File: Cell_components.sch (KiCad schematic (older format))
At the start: 12 parts, among them Q6 BUK9M20-40HX

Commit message: Add files via upload
Additional back-up before starting Rev.1
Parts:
- removed Q6: BUK9M20-40HX, Package_TO_SOT_SMD:LFPAK33, symbol Transistor_FET:BUK9M9R1-40EX
- added Q6: Q_NMOS_GSD, Package_TO_SOT_SMD:SOT-23, symbol Device:Q_NMOS_GSD
- C11, C12: DPN 710-885012207128 -> (none); LCSC (none) -> C49678
- D11, D12: DPN 771-PDZ5.6BGWJ -> (none); LCSC (none) -> C173406
- D16: footprint LED_SMD:LED_0603_1608Metric_Pad1.05x0.95mm_HandSolder -> LED_SMD:LED_0805_2012Metric_Pad1.15x1.40mm_HandSolder; LCSC (none) -> C2296
- R1, R3: DPN 603-RT0603FRE071KL -> (none); LCSC (none) -> C21190
- R19, R20: value 47 -> 51; DPN 652-CMP2512AFX-47R0L -> (none); LCSC (none) -> C41977
- R2: DPN 71-CRCW08051M00FKEAC -> (none); LCSC (none) -> C17514
- R31: value ?? -> 1k; DPN 603-RT0603FRE071KL -> (none); LCSC (none) -> C21190
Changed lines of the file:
@@
 $Descr User 7874 5906
 encoding utf-8
-Sheet 2 7
+Sheet 5 7
 Title ""
 Date ""
@@
 Comment4 ""
 $EndDescr
-$Comp
-L Transistor_FET:BUK9M9R1-40EX Q6
-U 1 1 5FB0C1EB
-P 3750 2200
-AR Path="/5FAA7870/5FB0C1EB" Ref="Q6"  Part="1"
-AR Path="/5FAF2B15/5FB0C1EB" Ref="Q2"  Part="1"
-AR Path="/5FB201DB/5FB0C1EB" Ref="Q1"  Part="1"
-AR Path="/5FB24C66/5FB0C1EB" Ref="Q3"  Part="1"
-AR Path="/5FA9BBC5/5FB0C1EB" Ref="Q4"  Part="1"
-AR Path="/5FA9D4E1/5FB0C1EB" Ref="Q5"  Part="1"
-F 0 "Q6" H 3600 2450 50  0000 L CNN
-F 1 "BUK9M20-40HX" H 3100 2350 50  0000 L CNN
-F 2 "Package_TO_SOT_SMD:LFPAK33" H 3950 2125 50  0001 L CIN
-F 3 "file:///C:/Users/HenkHenk/Downloads/BUK9M20-40H-1599146%20(1).pdf" V 3750 2200 50  0001 L CNN
-F 4 "771-BUK9M20-40HX" H 3750 2200 50  0001 C CNN "DPN"
-	1    3750 2200
-	-1   0    0    -1
-$EndComp
 Text HLabel 1700 1500 0    50   UnSpc ~ 0
 S+
@@
 AR Path="/5FA9BBC5/5FB16918" Ref="C8"  Part="1"
 AR Path="/5FA9D4E1/5FB16918" Ref="C10"  Part="1"
-F 0 "C12" H 1965 2096 50  0000 L CNN
+F 0 "C8" H 1965 2096 50  0000 L CNN
 F 1 "0.1u " H 1965 2005 50  0000 L CNN
 F 2 "Capacitor_SMD:C_0805_2012Metric_Pad1.15x1.40mm_HandSolder" H 1888 1900 50  0001 C CNN
 F 3 "file:///C:/Users/HenkHenk/Downloads/885012207128-1727772.pdf" H 1850 2050 50  0001 C CNN
-F 4 "710-885012207128" H 1850 2050 50  0001 C CNN "DPN"
+F 4 "C49678" H 1850 2050 50  0001 C CNN "LCSC"
 	1    1850 2050
 	1    0    0    -1
@@
 AR Path="/5FA9BBC5/5FB1FCF3" Ref="C7"  Part="1"
 AR Path="/5FA9D4E1/5FB1FCF3" Ref="C9"  Part="1"
-F 0 "C11" H 5365 1746 50  0000 L CNN
+F 0 "C7" H 5365 1746 50  0000 L CNN
 F 1 "0.1u " H 5365 1655 50  0000 L CNN
 F 2 "Capacitor_SMD:C_0805_2012Metric_Pad1.15x1.40mm_HandSolder" H 5288 1550 50  0001 C CNN
 F 3 "file:///C:/Users/HenkHenk/Downloads/885012207128-1727772.pdf" H 5250 1700 50  0001 C CNN
-F 4 "710-885012207128" H 5250 1700 50  0001 C CNN "DPN"
+F 4 "C49678" H 5250 1700 50  0001 C CNN "LCSC"
 	1    5250 1700
 	1    0    0    -1
@@
 AR Path="/5FA9D4E1/5FB211C7" Ref="R15"  Part="1"
 AR Path="/5FAA7870/5FB211C7" Ref="R18"  Part="1"
-F 0 "R18" V 5150 1450 50  0000 L CNN
+F 0 "R12" V 5150 1450 50  0000 L CNN
 F 1 "1K" V 5050 1450 50  0000 L CNN
 F 2 "Resistor_SMD:R_0603_1608Metric_Pad1.05x0.95mm_HandSolder" V 4880 1500 50  0001 C CNN
 F 3 "~" H 4950 1500 50  0001 C CNN
-F 4 "603-RT0603FRE071KL" V 4950 1500 50  0001 C CNN "DPN"
+F 4 "C21190" V 4950 1500 50  0001 C CNN "LCSC"
 	1    4950 1500
 	0    -1   -1   0
@@
 AR Path="/5FA9D4E1/5FB24803" Ref="R13"  Part="1"
 AR Path="/5FAA7870/5FB24803" Ref="R16"  Part="1"
-F 0 "R16" V 5150 2150 50  0000 L CNN
+F 0 "R10" V 5150 2150 50  0000 L CNN
 F 1 "1K" V 5050 2150 50  0000 L CNN
 F 2 "Resistor_SMD:R_0603_1608Metric_Pad1.05x0.95mm_HandSolder" V 4880 2200 50  0001 C CNN
 F 3 "~" H 4950 2200 50  0001 C CNN
-F 4 "603-RT0603FRE071KL" V 4950 2200 50  0001 C CNN "DPN"
+F 4 "C21190" V 4950 2200 50  0001 C CNN "LCSC"
 	1    4950 2200
 	0    -1   -1   0
@@
 AR Path="/5FA9D4E1/5FB273BA" Ref="R14"  Part="1"
 AR Path="/5FAA7870/5FB273BA" Ref="R17"  Part="1"
-F 0 "R17" H 4300 2350 50  0000 L CNN
+F 0 "R11" H 4300 2350 50  0000 L CNN
 F 1 "1M" H 4300 2450 50  0000 L CNN
 F 2 "Resistor_SMD:R_0805_2012Metric_Pad1.15x1.40mm_HandSolder" V 4430 2400 50  0001 C CNN
 F 3 "~" H 4500 2400 50  0001 C CNN
-F 4 "71-CRCW08051M00FKEAC" H 4500 2400 50  0001 C CNN "DPN"
+F 4 "C17514" H 4500 2400 50  0001 C CNN "LCSC"
 	1    4500 2400
 	-1   0    0    1
@@
 AR Path="/5FA9BBC5/5FB3410E" Ref="D7"  Part="1"
 AR Path="/5FA9D4E1/5FB3410E" Ref="D9"  Part="1"
-F 0 "D11" V 2354 2130 50  0000 L CNN
+F 0 "D7" V 2354 2130 50  0000 L CNN
 F 1 "5V6" V 2445 2130 50  0000 L CNN
 F 2 "Diode_SMD:D_SOD-123" H 2400 2050 50  0001 C CNN
 F 3 "file:///C:/Users/HenkHenk/Downloads/PDZ-GW_SER-1599748.pdf" H 2400 2050 50  0001 C CNN
-F 4 "771-PDZ5.6BGWJ" V 2400 2050 50  0001 C CNN "DPN"
+F 4 "C173406" V 2400 2050 50  0001 C CNN "LCSC"
 	1    2400 2050
 	0    1    1    0
@@
 AR Path="/5FA9BBC5/5FB35DA2" Ref="D8"  Part="1"
 AR Path="/5FA9D4E1/5FB35DA2" Ref="D10"  Part="1"
-F 0 "D12" V 4104 2480 50  0000 L CNN
+F 0 "D8" V 4104 2480 50  0000 L CNN
 F 1 "5V6" V 4195 2480 50  0000 L CNN
 F 2 "Diode_SMD:D_SOD-123" H 4150 2400 50  0001 C CNN
 F 3 "file:///C:/Users/HenkHenk/Downloads/PDZ-GW_SER-1599748.pdf" H 4150 2400 50  0001 C CNN
-F 4 "771-PDZ5.6BGWJ" V 4150 2400 50  0001 C CNN "DPN"
+F 4 "C173406" V 4150 2400 50  0001 C CNN "LCSC"
 	1    4150 2400
 	0    1    1    0
@@
 AR Path="/5FA9D4E1/5FAFC2A5" Ref="R28"  Part="1"
 AR Path="/5FAA7870/5FAFC2A5" Ref="R30"  Part="1"
-F 0 "R30" H 3500 1700 50  0000 L CNN
-F 1 "47" H 3500 1800 50  0000 L CNN
+F 0 "R26" H 3500 1700 50  0000 L CNN
+F 1 "51" H 3500 1800 50  0000 L CNN
 F 2 "Resistor_SMD:R_2512_6332Metric_Pad1.52x3.35mm_HandSolder" V 3580 1750 50  0001 C CNN
 F 3 "file:///C:/Users/HenkHenk/Downloads/cmp-a.pdf" H 3650 1750 50  0001 C CNN
-F 4 "652-CMP2512AFX-47R0L" V 3650 1750 50  0001 C CNN "DPN"
+F 4 "C41977" V 3650 1750 50  0001 C CNN "LCSC"
 	1    3650 1750
 	-1   0    0    1
@@
 AR Path="/5FA9D4E1/5FAFE41B" Ref="R27"  Part="1"
 AR Path="/5FAA7870/5FAFE41B" Ref="R29"  Part="1"
-F 0 "R29" H 3250 1700 50  0000 L CNN
-F 1 "47" H 3250 1800 50  0000 L CNN
+F 0 "R25" H 3250 1700 50  0000 L CNN
+F 1 "51" H 3250 1800 50  0000 L CNN
 F 2 "Resistor_SMD:R_2512_6332Metric_Pad1.52x3.35mm_HandSolder" V 3330 1750 50  0001 C CNN
 F 3 "file:///C:/Users/HenkHenk/Downloads/cmp-a.pdf" H 3400 1750 50  0001 C CNN
-F 4 "652-CMP2512AFX-47R0L" V 3400 1750 50  0001 C CNN "DPN"
+F 4 "C41977" V 3400 1750 50  0001 C CNN "LCSC"
 	1    3400 1750
 	-1   0    0    1
@@
 AR Path="/5FA9D4E1/5FB07EF1" Ref="R35"  Part="1"
 AR Path="/5FAA7870/5FB07EF1" Ref="R36"  Part="1"
-F 0 "R36" V 3050 1700 50  0000 L CNN
-F 1 "??" V 2950 1700 50  0000 L CNN
+F 0 "R34" V 3050 1700 50  0000 L CNN
+F 1 "1k" V 2950 1700 50  0000 L CNN
 F 2 "Resistor_SMD:R_0603_1608Metric_Pad1.05x0.95mm_HandSolder" V 2780 1750 50  0001 C CNN
 F 3 "~" H 2850 1750 50  0001 C CNN
-F 4 "603-RT0603FRE071KL" V 2850 1750 50  0001 C CNN "DPN"
+F 4 "C21190" V 2850 1750 50  0001 C CNN "LCSC"
 	1    2850 1750
 	-1   0    0    1
@@
 AR Path="/5FA9D4E1/5FB0934F" Ref="D17"  Part="1"
 AR Path="/5FAA7870/5FB0934F" Ref="D18"  Part="1"
-F 0 "D18" H 3093 1695 50  0000 C CNN
+F 0 "D16" H 3093 1695 50  0000 C CNN
 F 1 "LED" H 3093 1786 50  0000 C CNN
-F 2 "LED_SMD:LED_0603_1608Metric_Pad1.05x0.95mm_HandSolder" H 3100 1950 50  0001 C CNN
+F 2 "LED_SMD:LED_0805_2012Metric_Pad1.15x1.40mm_HandSolder" H 3100 1950 50  0001 C CNN
 F 3 "~" H 3100 1950 50  0001 C CNN
+F 4 "C2296" H 3100 1950 50  0001 C CNN "LCSC"
 	1    3100 1950
 	-1   0    0    1
@@
 	3250 1950 3400 1950
 Connection ~ 3400 1950
+$Comp
+L Device:Q_NMOS_GSD Q6
+U 1 1 601F5F7C
+P 3750 2200
+AR Path="/5FAA7870/601F5F7C" Ref="Q6"  Part="1"
+AR Path="/5FAF2B15/601F5F7C" Ref="Q1"  Part="1"
+AR Path="/5FB201DB/601F5F7C" Ref="Q2"  Part="1"
+AR Path="/5FB24C66/601F5F7C" Ref="Q3"  Part="1"
+AR Path="/5FA9BBC5/601F5F7C" Ref="Q4"  Part="1"
+AR Path="/5FA9D4E1/601F5F7C" Ref="Q5"  Part="1"
+F 0 "Q4" H 3955 2246 50  0000 L CNN
+F 1 "Q_NMOS_GSD" H 3955 2155 50  0000 L CNN
+F 2 "Package_TO_SOT_SMD:SOT-23" H 3950 2300 50  0001 C CNN
+F 3 "~" H 3750 2200 50  0001 C CNN
+F 4 "C20917" H 3750 2200 50  0001 C CNN "LCSC"
+	1    3750 2200
+	-1   0    0    -1
+$EndComp
 $EndSCHEMATC

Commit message: Add files via upload
Changed board dimensions. Replaced Molex connectors from MiniFit to the smaller MicroFit-type.
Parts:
- renumbered C12 to C23, C11 to C24, D16 to D11, D11 to D16, D12 to D18, R31 to R4, R19 to R5, R20 to R6, R2 to R7, R3 to R8, R1 to R9

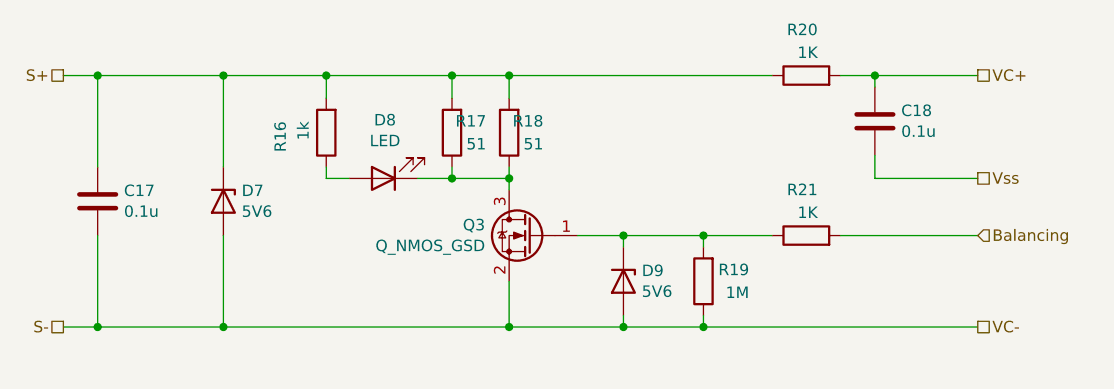
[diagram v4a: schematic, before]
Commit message: Add files via upload
Placed most components. Started routing and placing vias.
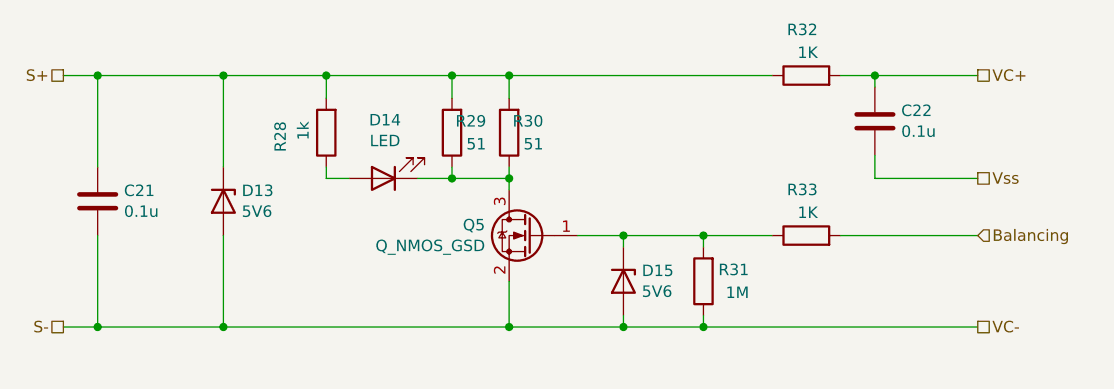
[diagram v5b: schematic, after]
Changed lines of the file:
@@
 $Descr User 7874 5906
 encoding utf-8
-Sheet 4 7
+Sheet 6 7
 Title ""
 Date ""
@@
 AR Path="/5FA9BBC5/5FB16918" Ref="C19"  Part="1"
 AR Path="/5FA9D4E1/5FB16918" Ref="C21"  Part="1"
-F 0 "C17" H 1965 2096 50  0000 L CNN
+F 0 "C21" H 1965 2096 50  0000 L CNN
 F 1 "0.1u " H 1965 2005 50  0000 L CNN
 F 2 "Capacitor_SMD:C_0805_2012Metric_Pad1.15x1.40mm_HandSolder" H 1888 1900 50  0001 C CNN
@@
 AR Path="/5FA9BBC5/5FB1FCF3" Ref="C20"  Part="1"
 AR Path="/5FA9D4E1/5FB1FCF3" Ref="C22"  Part="1"
-F 0 "C18" H 5365 1746 50  0000 L CNN
+F 0 "C22" H 5365 1746 50  0000 L CNN
 F 1 "0.1u " H 5365 1655 50  0000 L CNN
 F 2 "Capacitor_SMD:C_0805_2012Metric_Pad1.15x1.40mm_HandSolder" H 5288 1550 50  0001 C CNN
@@
 AR Path="/5FA9D4E1/5FB211C7" Ref="R32"  Part="1"
 AR Path="/5FAA7870/5FB211C7" Ref="R38"  Part="1"
-F 0 "R20" V 5150 1450 50  0000 L CNN
+F 0 "R32" V 5150 1450 50  0000 L CNN
 F 1 "1K" V 5050 1450 50  0000 L CNN
 F 2 "Resistor_SMD:R_0603_1608Metric_Pad1.05x0.95mm_HandSolder" V 4880 1500 50  0001 C CNN
@@
 AR Path="/5FA9D4E1/5FB24803" Ref="R33"  Part="1"
 AR Path="/5FAA7870/5FB24803" Ref="R39"  Part="1"
-F 0 "R21" V 5150 2150 50  0000 L CNN
+F 0 "R33" V 5150 2150 50  0000 L CNN
 F 1 "1K" V 5050 2150 50  0000 L CNN
 F 2 "Resistor_SMD:R_0603_1608Metric_Pad1.05x0.95mm_HandSolder" V 4880 2200 50  0001 C CNN
@@
 AR Path="/5FA9D4E1/5FB273BA" Ref="R31"  Part="1"
 AR Path="/5FAA7870/5FB273BA" Ref="R37"  Part="1"
-F 0 "R19" H 4300 2350 50  0000 L CNN
+F 0 "R31" H 4300 2350 50  0000 L CNN
 F 1 "1M" H 4300 2450 50  0000 L CNN
 F 2 "Resistor_SMD:R_0805_2012Metric_Pad1.15x1.40mm_HandSolder" V 4430 2400 50  0001 C CNN
@@
 AR Path="/5FA9BBC5/5FB35DA2" Ref="D12"  Part="1"
 AR Path="/5FA9D4E1/5FB35DA2" Ref="D15"  Part="1"
-F 0 "D9" V 4104 2480 50  0000 L CNN
+F 0 "D15" V 4104 2480 50  0000 L CNN
 F 1 "5V6" V 4195 2480 50  0000 L CNN
 F 2 "Diode_SMD:D_SOD-123" H 4150 2400 50  0001 C CNN
@@
 AR Path="/5FA9D4E1/5FAFC2A5" Ref="R30"  Part="1"
 AR Path="/5FAA7870/5FAFC2A5" Ref="R36"  Part="1"
-F 0 "R18" H 3500 1700 50  0000 L CNN
+F 0 "R30" H 3500 1700 50  0000 L CNN
 F 1 "51" H 3500 1800 50  0000 L CNN
 F 2 "Resistor_SMD:R_2512_6332Metric_Pad1.52x3.35mm_HandSolder" V 3580 1750 50  0001 C CNN
@@
 AR Path="/5FA9D4E1/5FAFE41B" Ref="R29"  Part="1"
 AR Path="/5FAA7870/5FAFE41B" Ref="R35"  Part="1"
-F 0 "R17" H 3250 1700 50  0000 L CNN
+F 0 "R29" H 3250 1700 50  0000 L CNN
 F 1 "51" H 3250 1800 50  0000 L CNN
 F 2 "Resistor_SMD:R_2512_6332Metric_Pad1.52x3.35mm_HandSolder" V 3330 1750 50  0001 C CNN
@@
 AR Path="/5FA9D4E1/5FB07EF1" Ref="R28"  Part="1"
 AR Path="/5FAA7870/5FB07EF1" Ref="R34"  Part="1"
-F 0 "R16" V 3050 1700 50  0000 L CNN
+F 0 "R28" V 3050 1700 50  0000 L CNN
 F 1 "1k" V 2950 1700 50  0000 L CNN
 F 2 "Resistor_SMD:R_0603_1608Metric_Pad1.05x0.95mm_HandSolder" V 2780 1750 50  0001 C CNN
@@
 AR Path="/5FA9D4E1/5FB0934F" Ref="D14"  Part="1"
 AR Path="/5FAA7870/5FB0934F" Ref="D17"  Part="1"
-F 0 "D8" H 3093 1695 50  0000 C CNN
+F 0 "D14" H 3093 1695 50  0000 C CNN
 F 1 "LED" H 3093 1786 50  0000 C CNN
 F 2 "LED_SMD:LED_0805_2012Metric_Pad1.15x1.40mm_HandSolder" H 3100 1950 50  0001 C CNN
@@
 AR Path="/5FA9BBC5/601F5F7C" Ref="Q4"  Part="1"
 AR Path="/5FA9D4E1/601F5F7C" Ref="Q5"  Part="1"
-F 0 "Q3" H 3955 2246 50  0000 L CNN
+F 0 "Q5" H 3955 2246 50  0000 L CNN
 F 1 "Q_NMOS_GSD" H 3955 2155 50  0000 L CNN
 F 2 "Package_TO_SOT_SMD:SOT-23" H 3950 2300 50  0001 C CNN
@@
 AR Path="/5FA9BBC5/5FB3410E" Ref="D10"  Part="1"
 AR Path="/5FA9D4E1/5FB3410E" Ref="D13"  Part="1"
-F 0 "D7" V 2354 2130 50  0000 L CNN
+F 0 "D13" V 2354 2130 50  0000 L CNN
 F 1 "5V6" V 2445 2130 50  0000 L CNN
 F 2 "Diode_SMD:D_SOD-123" H 2400 2050 50  0001 C CNN

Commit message: Add files via upload
Routed external thermistor and HOST-interface traces. Added silkscreen text. Placed additional AGND-via's.
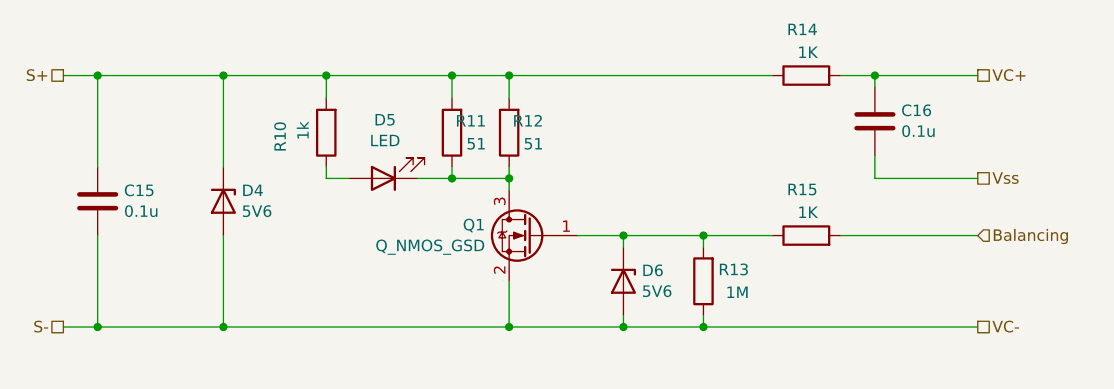
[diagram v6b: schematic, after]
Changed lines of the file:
@@
 $Descr User 7874 5906
 encoding utf-8
-Sheet 6 7
+Sheet 3 7
 Title ""
 Date ""
@@
 AR Path="/5FA9BBC5/5FB16918" Ref="C19"  Part="1"
 AR Path="/5FA9D4E1/5FB16918" Ref="C21"  Part="1"
-F 0 "C21" H 1965 2096 50  0000 L CNN
+F 0 "C15" H 1965 2096 50  0000 L CNN
 F 1 "0.1u " H 1965 2005 50  0000 L CNN
 F 2 "Capacitor_SMD:C_0805_2012Metric_Pad1.15x1.40mm_HandSolder" H 1888 1900 50  0001 C CNN
@@
 AR Path="/5FA9BBC5/5FB1FCF3" Ref="C20"  Part="1"
 AR Path="/5FA9D4E1/5FB1FCF3" Ref="C22"  Part="1"
-F 0 "C22" H 5365 1746 50  0000 L CNN
+F 0 "C16" H 5365 1746 50  0000 L CNN
 F 1 "0.1u " H 5365 1655 50  0000 L CNN
 F 2 "Capacitor_SMD:C_0805_2012Metric_Pad1.15x1.40mm_HandSolder" H 5288 1550 50  0001 C CNN
@@
 AR Path="/5FA9D4E1/5FB211C7" Ref="R32"  Part="1"
 AR Path="/5FAA7870/5FB211C7" Ref="R38"  Part="1"
-F 0 "R32" V 5150 1450 50  0000 L CNN
+F 0 "R14" V 5150 1450 50  0000 L CNN
 F 1 "1K" V 5050 1450 50  0000 L CNN
 F 2 "Resistor_SMD:R_0603_1608Metric_Pad1.05x0.95mm_HandSolder" V 4880 1500 50  0001 C CNN
@@
 AR Path="/5FA9D4E1/5FB24803" Ref="R33"  Part="1"
 AR Path="/5FAA7870/5FB24803" Ref="R39"  Part="1"
-F 0 "R33" V 5150 2150 50  0000 L CNN
+F 0 "R15" V 5150 2150 50  0000 L CNN
 F 1 "1K" V 5050 2150 50  0000 L CNN
 F 2 "Resistor_SMD:R_0603_1608Metric_Pad1.05x0.95mm_HandSolder" V 4880 2200 50  0001 C CNN
@@
 AR Path="/5FA9D4E1/5FB273BA" Ref="R31"  Part="1"
 AR Path="/5FAA7870/5FB273BA" Ref="R37"  Part="1"
-F 0 "R31" H 4300 2350 50  0000 L CNN
+F 0 "R13" H 4300 2350 50  0000 L CNN
 F 1 "1M" H 4300 2450 50  0000 L CNN
 F 2 "Resistor_SMD:R_0805_2012Metric_Pad1.15x1.40mm_HandSolder" V 4430 2400 50  0001 C CNN
@@
 AR Path="/5FA9BBC5/5FB35DA2" Ref="D12"  Part="1"
 AR Path="/5FA9D4E1/5FB35DA2" Ref="D15"  Part="1"
-F 0 "D15" V 4104 2480 50  0000 L CNN
+F 0 "D6" V 4104 2480 50  0000 L CNN
 F 1 "5V6" V 4195 2480 50  0000 L CNN
 F 2 "Diode_SMD:D_SOD-123" H 4150 2400 50  0001 C CNN
@@
 AR Path="/5FA9D4E1/5FAFC2A5" Ref="R30"  Part="1"
 AR Path="/5FAA7870/5FAFC2A5" Ref="R36"  Part="1"
-F 0 "R30" H 3500 1700 50  0000 L CNN
+F 0 "R12" H 3500 1700 50  0000 L CNN
 F 1 "51" H 3500 1800 50  0000 L CNN
 F 2 "Resistor_SMD:R_2512_6332Metric_Pad1.52x3.35mm_HandSolder" V 3580 1750 50  0001 C CNN
@@
 AR Path="/5FA9D4E1/5FAFE41B" Ref="R29"  Part="1"
 AR Path="/5FAA7870/5FAFE41B" Ref="R35"  Part="1"
-F 0 "R29" H 3250 1700 50  0000 L CNN
+F 0 "R11" H 3250 1700 50  0000 L CNN
 F 1 "51" H 3250 1800 50  0000 L CNN
 F 2 "Resistor_SMD:R_2512_6332Metric_Pad1.52x3.35mm_HandSolder" V 3330 1750 50  0001 C CNN
@@
 AR Path="/5FA9D4E1/5FB07EF1" Ref="R28"  Part="1"
 AR Path="/5FAA7870/5FB07EF1" Ref="R34"  Part="1"
-F 0 "R28" V 3050 1700 50  0000 L CNN
+F 0 "R10" V 3050 1700 50  0000 L CNN
 F 1 "1k" V 2950 1700 50  0000 L CNN
 F 2 "Resistor_SMD:R_0603_1608Metric_Pad1.05x0.95mm_HandSolder" V 2780 1750 50  0001 C CNN
@@
 AR Path="/5FA9D4E1/5FB0934F" Ref="D14"  Part="1"
 AR Path="/5FAA7870/5FB0934F" Ref="D17"  Part="1"
-F 0 "D14" H 3093 1695 50  0000 C CNN
+F 0 "D5" H 3093 1695 50  0000 C CNN
 F 1 "LED" H 3093 1786 50  0000 C CNN
 F 2 "LED_SMD:LED_0805_2012Metric_Pad1.15x1.40mm_HandSolder" H 3100 1950 50  0001 C CNN
@@
 AR Path="/5FA9BBC5/601F5F7C" Ref="Q4"  Part="1"
 AR Path="/5FA9D4E1/601F5F7C" Ref="Q5"  Part="1"
-F 0 "Q5" H 3955 2246 50  0000 L CNN
+F 0 "Q1" H 3955 2246 50  0000 L CNN
 F 1 "Q_NMOS_GSD" H 3955 2155 50  0000 L CNN
 F 2 "Package_TO_SOT_SMD:SOT-23" H 3950 2300 50  0001 C CNN
@@
 AR Path="/5FA9BBC5/5FB3410E" Ref="D10"  Part="1"
 AR Path="/5FA9D4E1/5FB3410E" Ref="D13"  Part="1"
-F 0 "D13" V 2354 2130 50  0000 L CNN
+F 0 "D4" V 2354 2130 50  0000 L CNN
 F 1 "5V6" V 2445 2130 50  0000 L CNN
 F 2 "Diode_SMD:D_SOD-123" H 2400 2050 50  0001 C CNN
